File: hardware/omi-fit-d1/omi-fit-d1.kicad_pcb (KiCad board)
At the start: 4 copper layers, 23 x 23 mm, 76 parts, among them J1 USB4105-GF-A (candidate), J2 SM02B-SRSS-TB / factory prote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, J3 TC2030 SWD target pads, Q1 DMP2035U (candidate; power pa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, Q2 2N7002 (charge inhibit), Q3 2N7002 (VBUS detect), SW1 B3U-1000P (candidate), U1 STM32U535CEU6, U10 TPS22916CYFPR, U11 CSNP32GCR01-BOW, U2 USBLC6-2P6, U3 BQ25101YFPR, U4 TPS7A0233PDBVR, U6 TPS7A0218PDBVR, U8 T5838, U9 TXS0104ERUTR, Y1 32.768kHz CL=7pF TBD

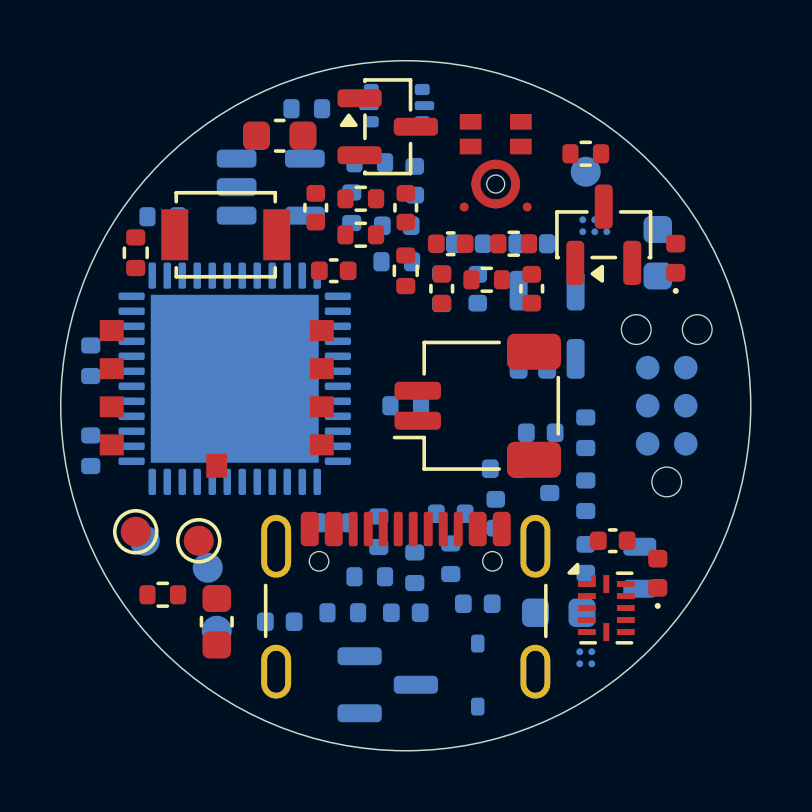
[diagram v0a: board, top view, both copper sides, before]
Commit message: Add pendant case retention and acoustic duct; record partial routing and order gates
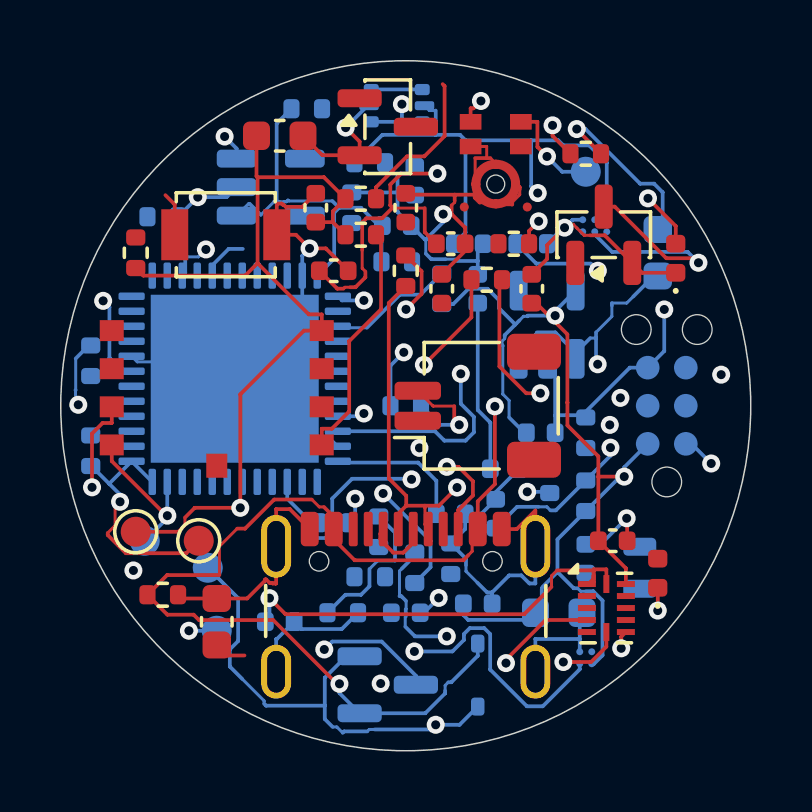
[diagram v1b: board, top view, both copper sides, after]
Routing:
- net /GND: track 0.00 -> 116.0 mm, vias 0 -> 15
- net /V3V3: track 0.00 -> 82.9 mm, vias 0 -> 3
- net /VBUS: track 0.00 -> 58.9 mm, vias 0 -> 3
- net /SD_V3: track 0.00 -> 54.8 mm, vias 0 -> 2
- net /V1V8: track 0.00 -> 49.7 mm, vias 0 -> 3
- net /SYS: track 0.00 -> 41.6 mm, vias 0 -> 2
- net /MIC_DATA_1V8: track 0.00 -> 32.4 mm, vias 0 -> 2
- net /NRST: track 0.00 -> 28.9 mm, vias 0 -> 2
- net /USB_DP: track 0.00 -> 27.8 mm, vias 0 -> 2
- net /SD_CLK: track 0.00 -> 23.5 mm, vias 0 -> 4
- net /BAT_TS: track 0.00 -> 21.1 mm, vias 0 -> 2
- net /SWDIO: track 0.00 -> 20.5 mm, vias 0 -> 3
- net /PDM_CLK: track 0.00 -> 18.6 mm, vias 0 -> 3
- net /CC2: track 0.00 -> 17.2 mm, vias 0 -> 3
- net /SD_CLK_MCU: track 0.00 -> 15.9 mm, vias 0 -> 2
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- added copper zone on In1.Cu, net /GND

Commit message: Route circular D1.1 and prepare unreleased DFM package
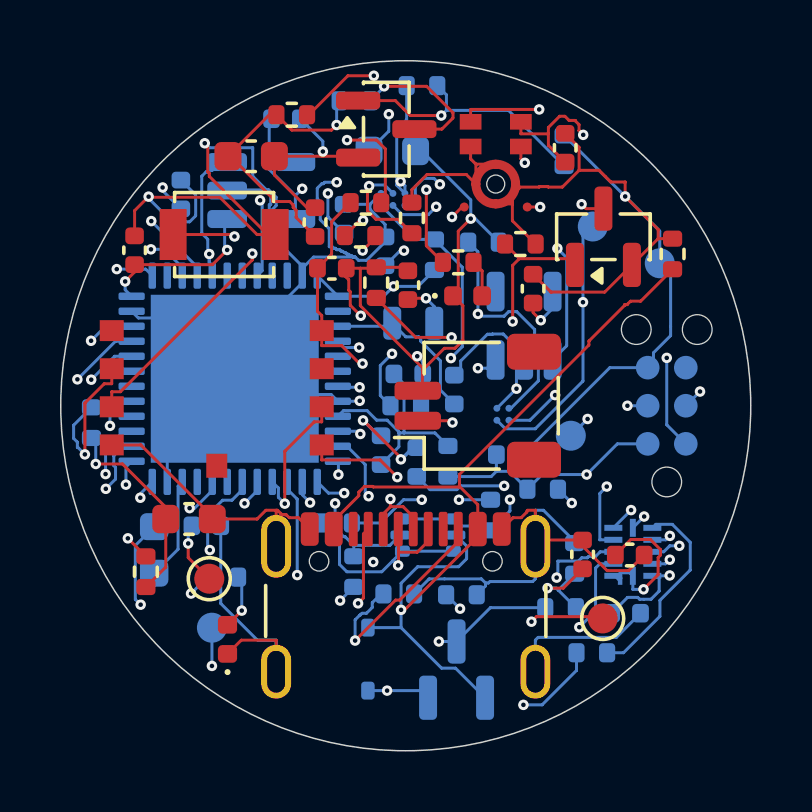
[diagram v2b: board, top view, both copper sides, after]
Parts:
- C11, C14, C18, C19, C5, R21, R28, R32, R8, TP5, U9: moved to B.Cu
- C12, C16, C2, C22, C28, C4, R10, R12, R23, R4, R5, TP2: moved to F.Cu
- J1: footprint Connector_USB:USB_C_Receptacle_GCT_USB4105-xx-A_16P_TopMnt_Horizontal -> PendantD1:USB_C_GCT_USB4105_GroundLand112
- moved R16 20.4 mm to (108.9, 94.9), turned to 90 degrees
- moved D6 19.6 mm to (94.1, 107.8)
- moved TP6 19.5 mm to (108.5, 95.3), turned to 90 degrees
- moved C19 18.5 mm to (92.5, 93.0), turned to 90 degrees
- moved C22 18.4 mm to (105.3, 91.4), turned to 90 degrees
- moved C4 18.3 mm to (94.8, 91.7)
- moved TP5 18.3 mm to (106.2, 94.0), turned to 90 degrees
- moved C24 15.0 mm to (107.3, 106.9)
- moved C2 14.8 mm to (91.0, 94.8), turned to 90 degrees
- moved R32 14.7 mm to (93.9, 105.7)
- moved R14 14.6 mm to (105.3, 91.5), turned to 90 degrees
- moved U2 14.4 mm to (100.7, 104.3)
- moved C23 13.7 mm to (107.5, 105.0)
- moved TP2 13.3 mm to (106.6, 107.1)
- moved C27 13.1 mm to (92.8, 103.8)
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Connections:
- U1 pad 19: /MIC_EN -> unconnected-(U1-PB1-Pad19)
- U1 pad 41: unconnected-(U1-PB5-Pad41) -> /MIC_EN
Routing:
- net /GND: track 116.0 -> 179.9 mm
- net /PDM_DATA: track 0.00 -> 29.3 mm, vias 0 -> 2
- net /BAT: track 9.63 -> 38.7 mm, vias 2 -> 5
- net /SD_EN: track 0.00 -> 26.9 mm, vias 0 -> 2
- net /SWCLK: track 0.00 -> 23.6 mm, vias 0 -> 2
- net /BUTTON_N: track 1.47 -> 25.0 mm, vias 0 -> 3
- net /CHG_DISABLE: track 0.00 -> 19.4 mm, vias 0 -> 2
- net /VBUS_N: track 0.00 -> 19.0 mm, vias 0 -> 2
- net /MIC_WAKE_1V8: track 0.00 -> 19.0 mm, vias 0 -> 2
- net /USB_DP: track 27.8 -> 8.82 mm, vias 2 -> 1
- net /BOOT0: track 0.00 -> 17.7 mm, vias 0 -> 2
- net /CHG_N: track 4.23 -> 21.8 mm, vias 0 -> 2
- net /USB_DM_MCU: track 0.00 -> 16.6 mm, vias 0 -> 2
- net /MIC_THSEL_1V8: track 0.00 -> 15.8 mm, vias 0 -> 2
- net /SD_MOSI: track 9.68 -> 25.1 mm, vias 0 -> 3
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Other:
- copper layers 4 -> 6
